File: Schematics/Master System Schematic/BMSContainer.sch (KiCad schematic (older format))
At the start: 2 parts, among them U1 OrionBMS2, U2 OrionThermExp

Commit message: BMS Schematic Edits 1
Added BMS2V2 component
Updated Thermistor Expansion
Cleaned up BMSContainer schematic
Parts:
- removed U1: OrionBMS2, symbol NER:OrionBMS2
- added U1: OrionBMS2v2, symbol NER:OrionBMS2v2
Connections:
- net labels removed: ChargeSafety
- wire segments 77 -> 60
- no-connect marks 2 -> 3
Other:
- moved on the sheet: U2

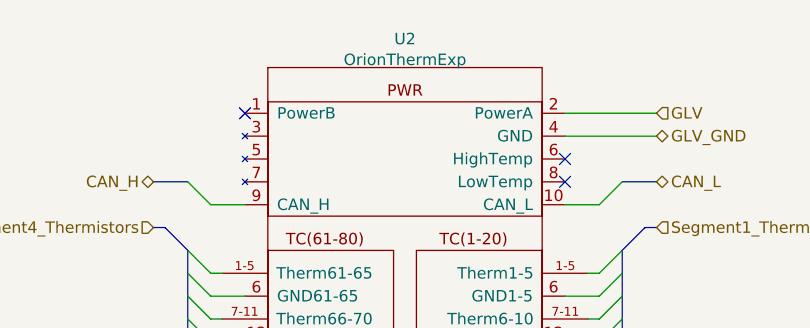
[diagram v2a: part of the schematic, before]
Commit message: Connected new BMS schematic to master schematic
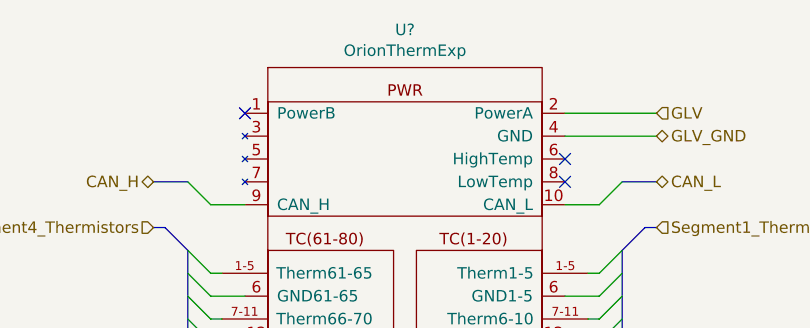
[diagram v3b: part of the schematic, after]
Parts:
- removed U2: OrionThermExp, symbol NER:OrionThermExp
- added U?: OrionThermExp, symbol NER:OrionThermExp
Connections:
- net GLV: now also U?.2 (PowerA)
- net GLV_GND: now also U?.4 (GND)
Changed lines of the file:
@@
 $Descr A 11000 8500
 encoding utf-8
-Sheet 1 1
+Sheet 4 17
 Title ""
 Date "2020-10-12"
@@
 	1    0    0    -1
 $EndComp
-$Comp
-L NER:OrionThermExp U2
-U 1 1 60D555EB
-P 7900 1900
-F 0 "U2" H 7900 2025 50  0000 C CNN
-F 1 "OrionThermExp" H 7900 1934 50  0000 C CNN
-F 2 "" H 7900 1900 50  0001 C CNN
-F 3 "" H 7900 1900 50  0001 C CNN
-	1    7900 1900
-	1    0    0    -1
-$EndComp
 Text HLabel 4650 3550 2    50   Input ~ 0
 Current_Sensor
@@
 Wire Bus Line
 	8850 3750 8850 4450
+$Comp
+L NER:OrionThermExp U?
+U 1 1 5F8ADC5C
+P 7900 1900
+F 0 "U?" H 7900 2065 50  0000 C CNN
+F 1 "OrionThermExp" H 7900 1974 50  0000 C CNN
+F 2 "" H 7900 1800 50  0001 C CNN
+F 3 "" H 7900 1800 50  0001 C CNN
+	1    7900 1900
+	1    0    0    -1
+$EndComp
 $EndSCHEMATC

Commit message: Cleanup
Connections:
- net BMS_Fault: now also U1.26 (MP_En)
- no-connect marks 3 -> 24
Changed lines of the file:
@@
 $Descr A 11000 8500
 encoding utf-8
-Sheet 4 17
+Sheet 1 1
 Title ""
 Date "2020-10-12"
@@
 Text HLabel 9000 2200 2    50   BiDi ~ 0
 GLV_GND
-Text HLabel 1950 4350 0    50   Input ~ 0
+Text HLabel 1950 4750 0    50   Input ~ 0
 BMS_Fault
 Text HLabel 6800 2400 0    50   BiDi ~ 0
@@
 NoConn ~ 8600 2400
 NoConn ~ 7200 2100
-Wire Bus Line
-	4500 4000 4500 4300
-Wire Bus Line
-	4500 4400 4500 5200
-Wire Bus Line
-	4500 5300 4500 5600
-Wire Bus Line
-	2100 5100 2100 5400
-Wire Bus Line
-	8850 2700 8850 3400
-Wire Bus Line
-	6950 2700 6950 3400
-Wire Bus Line
-	6950 3750 6950 4450
-Wire Bus Line
-	8850 3750 8850 4450
 $Comp
 L NER:OrionThermExp U?
@@
 	1    0    0    -1
 $EndComp
+Wire Wire Line
+	1950 4750 2350 4750
+NoConn ~ 2350 2250
+NoConn ~ 2350 2450
+NoConn ~ 2350 2550
+NoConn ~ 2350 2650
+NoConn ~ 2350 2750
+NoConn ~ 2350 2850
+NoConn ~ 2350 2950
+NoConn ~ 2350 3050
+NoConn ~ 2350 3150
+NoConn ~ 2350 3450
+NoConn ~ 2350 3550
+NoConn ~ 2350 3650
+NoConn ~ 2350 3750
+NoConn ~ 2350 3850
+NoConn ~ 2350 4150
+NoConn ~ 2350 4250
+NoConn ~ 2350 4350
+NoConn ~ 2350 4450
+NoConn ~ 2350 4550
+NoConn ~ 2250 5600
+NoConn ~ 2350 5700
+Wire Bus Line
+	4500 4000 4500 4300
+Wire Bus Line
+	4500 4400 4500 5200
+Wire Bus Line
+	4500 5300 4500 5600
+Wire Bus Line
+	2100 5100 2100 5400
+Wire Bus Line
+	8850 2700 8850 3400
+Wire Bus Line
+	6950 2700 6950 3400
+Wire Bus Line
+	6950 3750 6950 4450
+Wire Bus Line
+	8850 3750 8850 4450
 $EndSCHEMATC

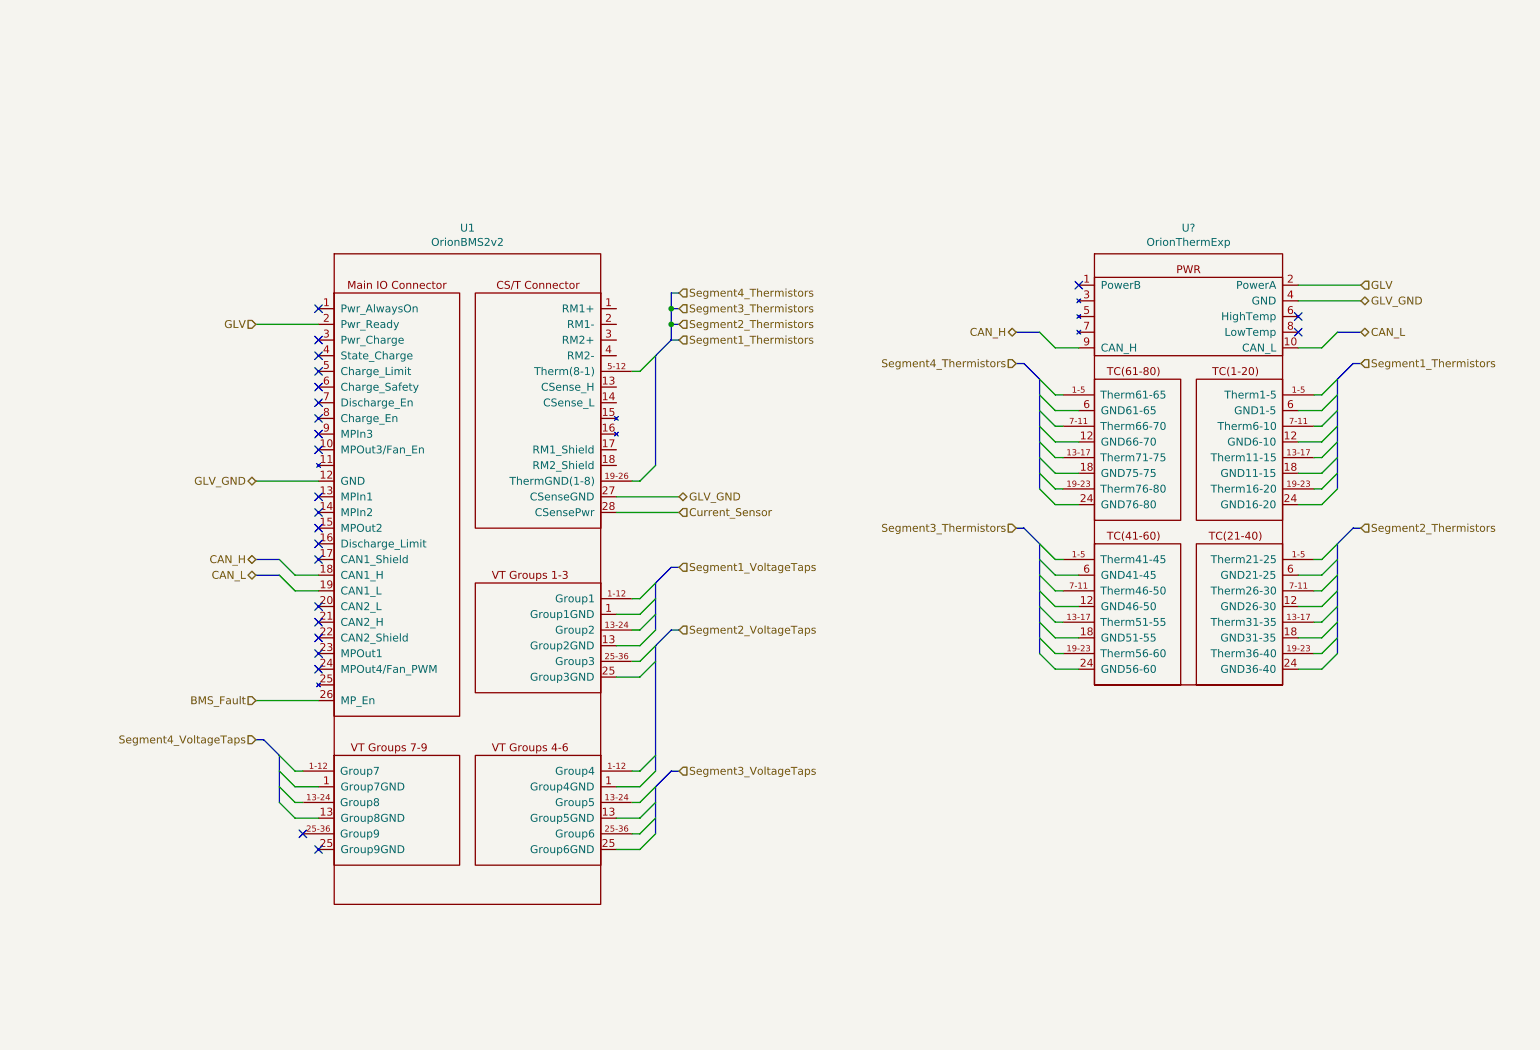
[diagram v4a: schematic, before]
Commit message: Fixed CAN
Changed to represent one connection. This ofc can be changed back if you meant to imply two CAN connections coming in
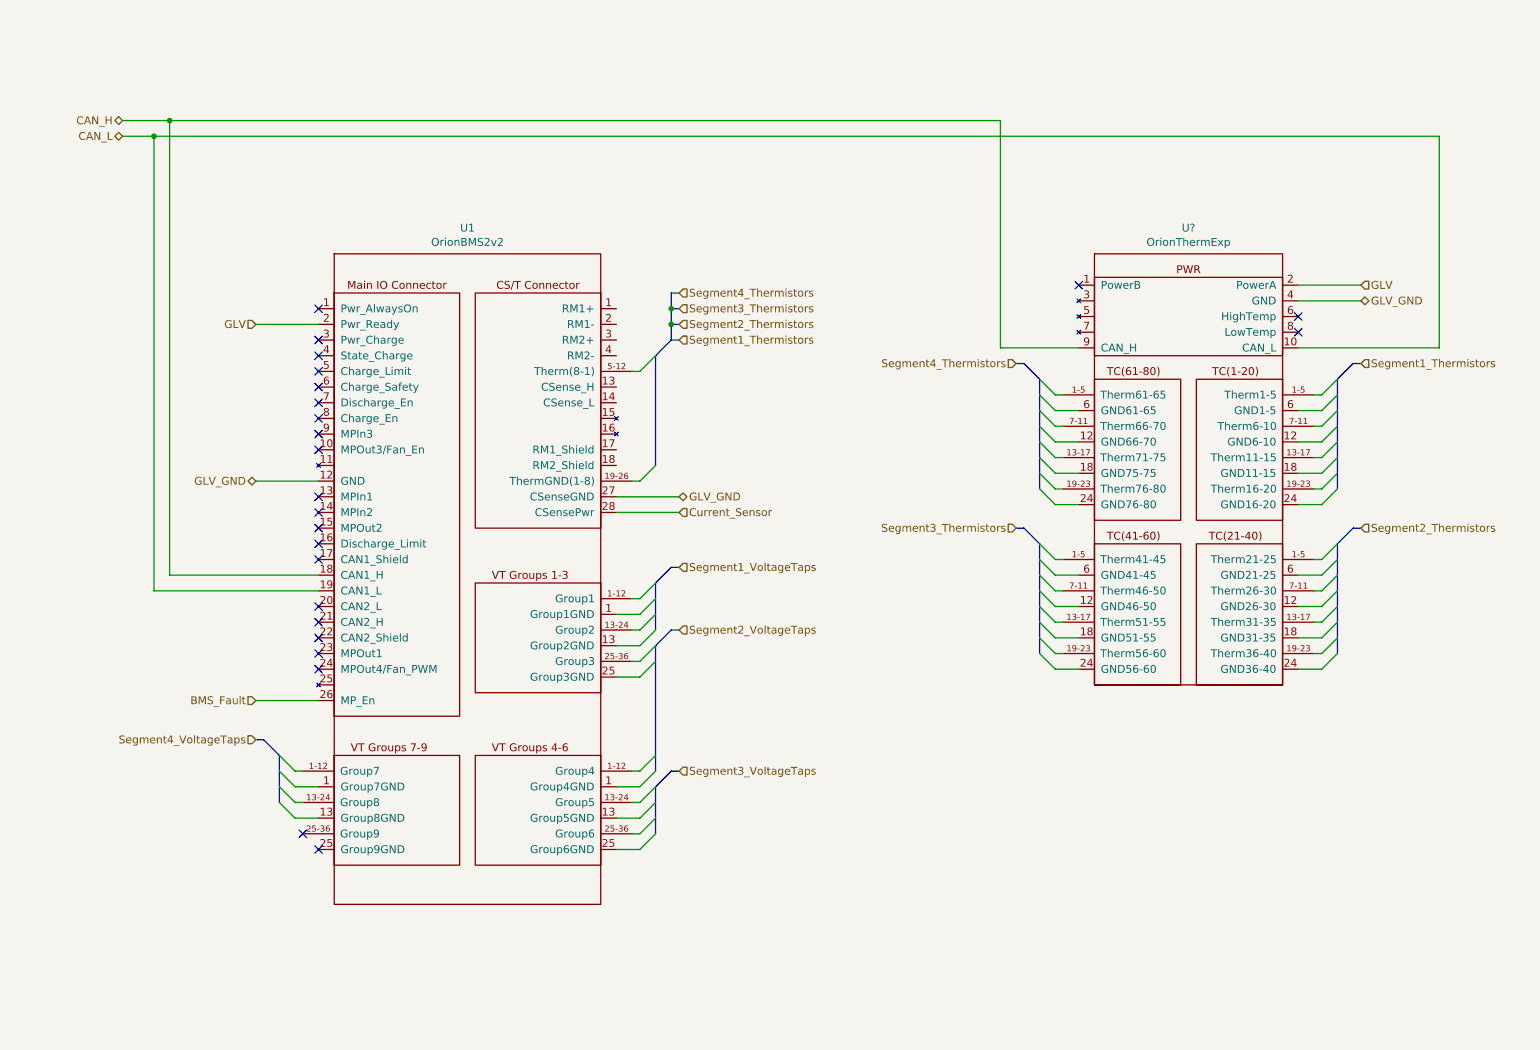
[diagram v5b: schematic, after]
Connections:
- net CAN_H: now also U1.18 (RM2_Shield), U?.9 (CAN_H)
- net CAN_L: now also U1.19 (CAN1_L), U?.10 (CAN_L)
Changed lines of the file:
@@
 EESchema Schematic File Version 4
+LIBS:Master System Schematic-cache
 EELAYER 30 0
 EELAYER END
 $Descr A 11000 8500
 encoding utf-8
-Sheet 1 1
+Sheet 4 17
 Title ""
 Date "2020-10-12"
@@
 Text HLabel 6800 3650 0    50   Input ~ 0
 Segment3_Thermistors
-Text HLabel 1950 3850 0    50   BiDi ~ 0
+Text HLabel 1100 1050 0    50   BiDi ~ 0
 CAN_H
-Text HLabel 1950 3950 0    50   BiDi ~ 0
+Text HLabel 1100 1150 0    50   BiDi ~ 0
 CAN_L
 Text HLabel 1950 2350 0    50   Input ~ 0
@@
 Entry Bus Bus
 	8850 3750 8950 3650
-Entry Wire Line
-	6950 2400 7050 2500
-Text HLabel 9000 2400 2    50   BiDi ~ 0
-CAN_L
-Wire Bus Line
-	6800 2400 6950 2400
-Wire Bus Line
-	8850 2400 9000 2400
 Text HLabel 9000 2200 2    50   BiDi ~ 0
 GLV_GND
 Text HLabel 1950 4750 0    50   Input ~ 0
 BMS_Fault
-Text HLabel 6800 2400 0    50   BiDi ~ 0
-CAN_H
 Text HLabel 6800 2600 0    50   Input ~ 0
 Segment4_Thermistors
 Entry Wire Line
 	7050 3500 6950 3400
-Entry Wire Line
-	8850 2400 8750 2500
 Wire Wire Line
 	7050 2800 7100 2800
@@
 Wire Wire Line
 	8700 2800 8750 2800
-Wire Wire Line
-	8750 2500 8600 2500
-Wire Wire Line
-	7050 2500 7200 2500
 Wire Wire Line
 	9000 2200 8600 2200
@@
 Wire Bus Line
 	2000 5000 1950 5000
-Entry Wire Line
-	2100 3850 2200 3950
-Wire Wire Line
-	2200 3950 2350 3950
-Entry Wire Line
-	2100 3950 2200 4050
-Wire Wire Line
-	2200 4050 2350 4050
-Wire Bus Line
-	1950 3850 2100 3850
-Wire Bus Line
-	1950 3950 2100 3950
 Wire Wire Line
 	1950 3350 2350 3350
@@
 NoConn ~ 2250 5600
 NoConn ~ 2350 5700
+Wire Wire Line
+	1100 1050 1400 1050
+Wire Wire Line
+	1400 1050 1400 3950
+Wire Wire Line
+	1100 1150 1300 1150
+Wire Wire Line
+	1300 1150 1300 4050
+Wire Wire Line
+	1300 4050 2350 4050
+Wire Wire Line
+	1400 1050 6700 1050
+Wire Wire Line
+	6700 1050 6700 2500
+Connection ~ 1400 1050
+Wire Wire Line
+	1300 1150 9500 1150
+Wire Wire Line
+	9500 1150 9500 2500
+Wire Wire Line
+	8600 2500 9500 2500
+Connection ~ 1300 1150
+Wire Wire Line
+	6700 2500 7200 2500
+Wire Wire Line
+	1400 3950 2350 3950
 Wire Bus Line
 	4500 4000 4500 4300

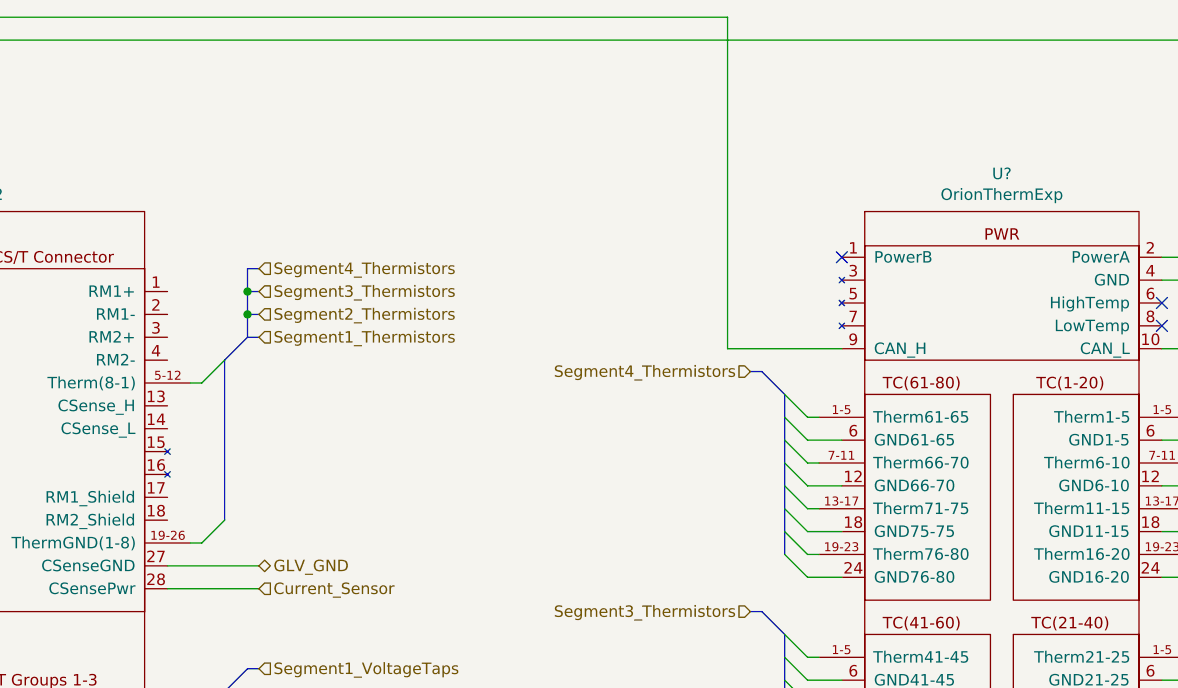
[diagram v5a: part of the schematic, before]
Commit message: Final cleanup
Fixed some no-connects
Annotated
Added revision number and title information
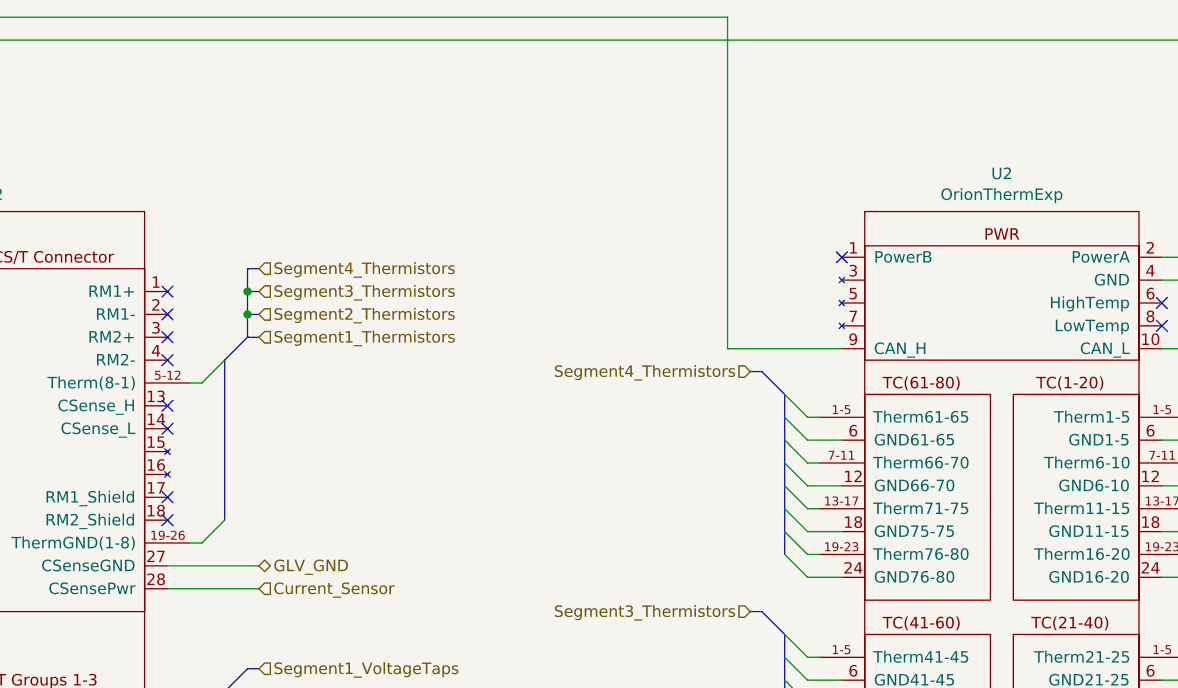
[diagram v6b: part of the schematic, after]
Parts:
- gave numbers to parts that had none: 1
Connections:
- no-connect marks 24 -> 32
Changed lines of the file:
@@
 EESchema Schematic File Version 4
-LIBS:Master System Schematic-cache
 EELAYER 30 0
 EELAYER END
 $Descr A 11000 8500
 encoding utf-8
-Sheet 4 17
-Title ""
-Date "2020-10-12"
-Rev ""
-Comp ""
-Comment1 ""
+Sheet 1 1
+Title "BMS Container Schematic"
+Date "2020-10-16"
+Rev "1"
+Comp "Northeaster Electric Racing"
+Comment1 "Dylan Gardner, Zack Perry"
 Comment2 ""
 Comment3 ""
@@
 NoConn ~ 7200 2100
 $Comp
-L NER:OrionThermExp U?
+L NER:OrionThermExp U2
 U 1 1 5F8ADC5C
 P 7900 1900
-F 0 "U?" H 7900 2065 50  0000 C CNN
+F 0 "U2" H 7900 2065 50  0000 C CNN
 F 1 "OrionThermExp" H 7900 1974 50  0000 C CNN
 F 2 "" H 7900 1800 50  0001 C CNN
@@
 Wire Wire Line
 	1400 3950 2350 3950
+NoConn ~ 4250 2250
+NoConn ~ 4250 2350
+NoConn ~ 4250 2450
+NoConn ~ 4250 2550
+NoConn ~ 4250 2750
+NoConn ~ 4250 2850
+NoConn ~ 4250 3150
+NoConn ~ 4250 3250
 Wire Bus Line
 	4500 4000 4500 4300
